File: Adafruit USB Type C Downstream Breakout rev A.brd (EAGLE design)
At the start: 20.3 x 14 mm, 10 parts

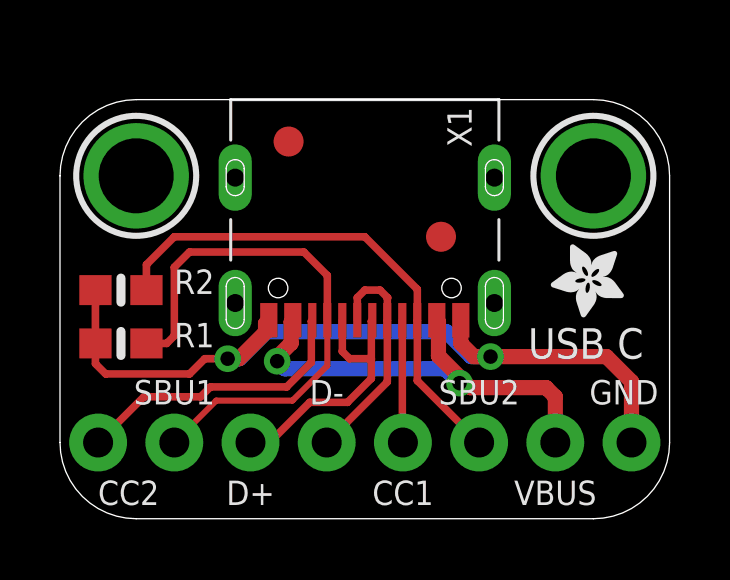
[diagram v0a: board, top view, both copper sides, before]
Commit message: Move the USB-C port proud of the board to make it easier to include in other projects.
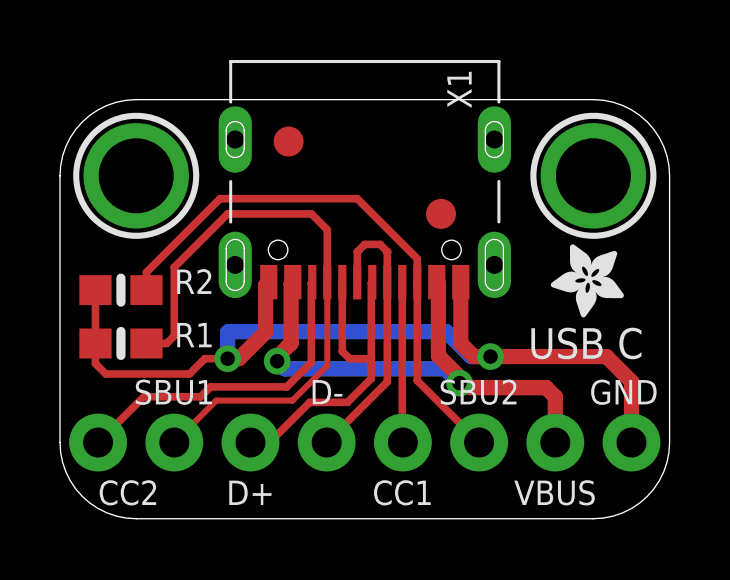
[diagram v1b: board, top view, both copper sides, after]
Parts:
- moved X1 1.27 mm to (10.2, 15.2)
- moved FID1 0.76 mm to (12.7, 10.2)
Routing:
- net GND: track 27.8 -> 30.8 mm
- net VBUS: track 15.3 -> 17.8 mm
- net D+: track 8.97 -> 11.5 mm
- net SBU1: track 18.1 -> 20.1 mm
- net D-: track 7.64 -> 9.42 mm
- net SBU2: track 16.9 -> 18.4 mm
- net CC2: track 9.63 -> 10.9 mm
- net CC1: track 4.08 -> 5.35 mm
